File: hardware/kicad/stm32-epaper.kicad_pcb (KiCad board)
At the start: 4 copper layers, 97.4 x 60 mm, 155 parts, among them J1 USB_C_Receptacle_USB2.0_16P, J101 TC2050-IDC-NL, J102 UART (TX RX GND), J2 BATT (1S LiPo), J201 microSD, J301 IT8951 HAT, J302 Electrodes L, J303 Electrodes R, SW101 BOOT, SW301 PEC11R-4220F-S0024, SW302 POWER, U1 BQ24073RGT, U101 STM32F469IIT6, U2 TPS63802DLA, U201 IS42S16400J-6TLI, U202 W25Q128JVSIQ, U3 TPS61023DRL, U301 CAP1188-1-CP-TR, U302 TPD4E05U06DQAR, U4 TPS22965DSG, U5 USBLC6-2SC6, U6 TPS63900DSK, U7 MCP1700T-3002E/TT, Y101 8MHz CL8pF, Y102 32.768kHz CL6pF

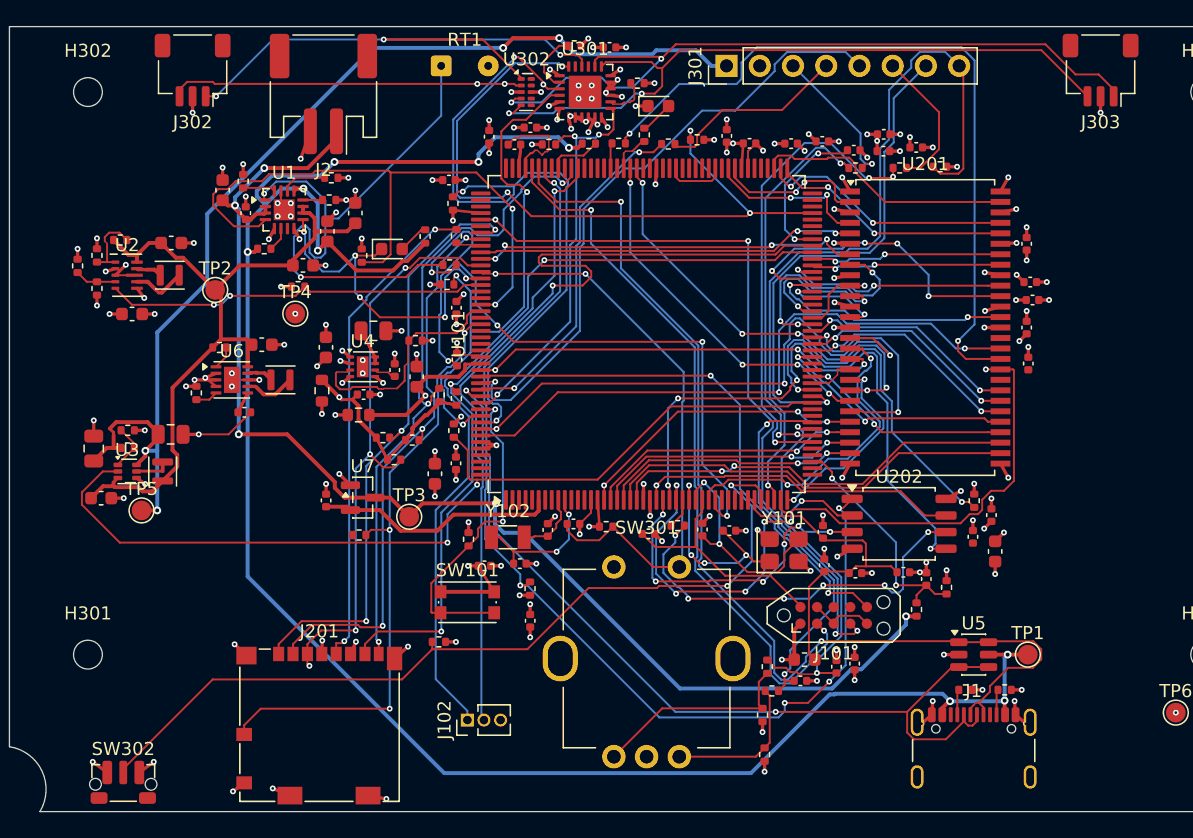
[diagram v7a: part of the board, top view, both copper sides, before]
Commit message: Routing attempt 8: 13 unconnected / 5 nets - all MCU power pins connect
MCU power vias perpendicular-inward under the LQFP body. Bus lengths got
worse (vias under the body block those paths); 3V3_AON split by the
3V3_PERIPH strip; touch escapes blocked above the CAP1188.

Co-Authored-By: Claude Opus 5.5 <noreply@anthropic.com>
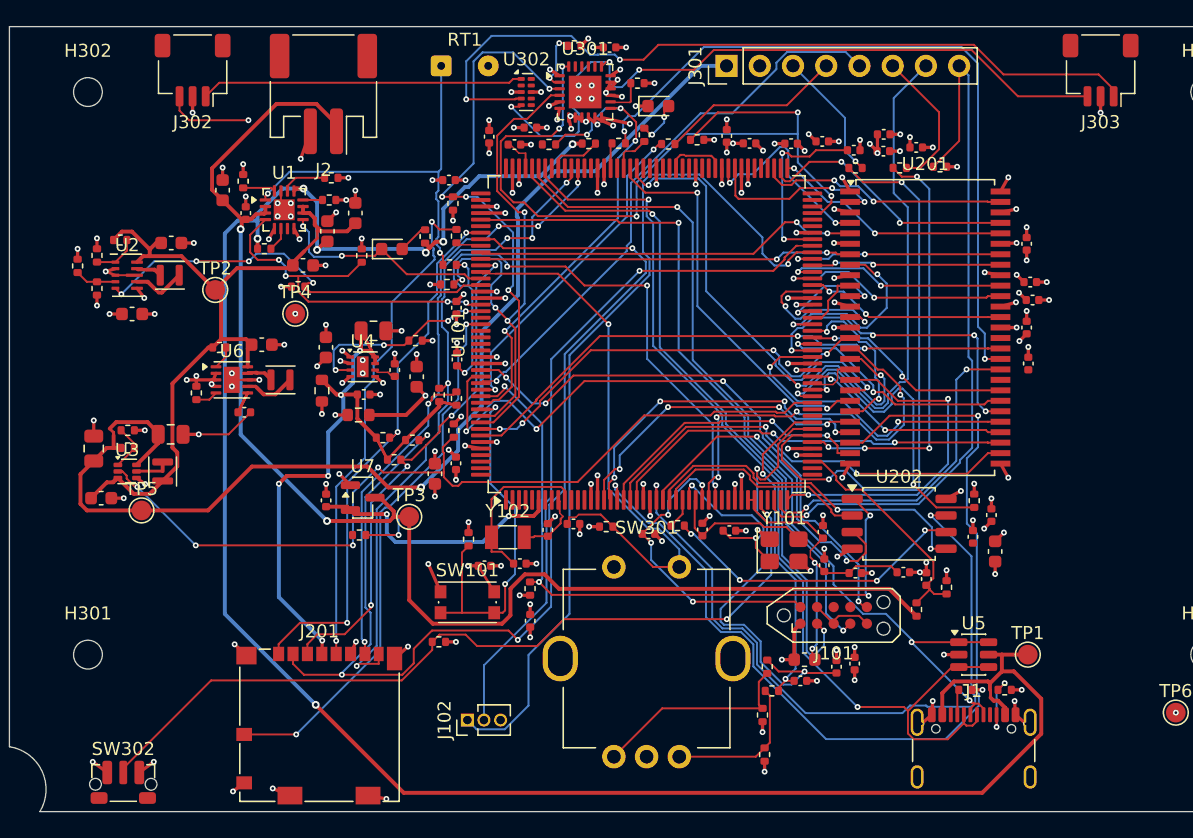
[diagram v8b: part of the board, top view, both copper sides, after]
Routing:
- net FMC_A2: track 20.3 -> 74.9 mm
- net SDIO_D3: track 43.2 -> 89.2 mm, vias 3 -> 4
- net 3V3_PERIPH: track 43.7 -> 75.2 mm, vias 20 -> 23
- net QUADSPI_BK1_IO3: track 24.8 -> 54.4 mm, vias 1 -> 2
- net /Peripherals/TOUCH_L2: track 27.0 -> 6.67 mm, vias 2 -> 1
- net QUADSPI_BK1_IO0: track 46.4 -> 26.6 mm, vias 4 -> 2
- net CHG_DIS: track 48.2 -> 28.7 mm, vias 2 -> 4
- net /Peripherals/TOUCH_L1: track 43.5 -> 24.7 mm, vias 3 -> 0
- net /Power/TS: track 45.7 -> 30.0 mm
- net SPI1_SCK: track 29.9 -> 44.2 mm, vias 3 -> 2
- net QUADSPI_BK1_IO1: track 30.3 -> 16.6 mm, vias 6 -> 0
- net /MCU/USART3_RX: track 66.6 -> 53.4 mm
- net I2C1_SDA: track 55.5 -> 42.7 mm
- net USB_DP: track 81.0 -> 68.9 mm, vias 2 -> 3
- net FMC_SDNE0: track 15.3 -> 26.6 mm
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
